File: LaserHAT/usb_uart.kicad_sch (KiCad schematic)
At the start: 9 parts

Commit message: Updates with lots of manual work
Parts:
- removed C_USB1, C_USB2: 100nF, Capacitor_SMD:C_0402_1005Metric, symbol Device:C
- removed J_USB: USB_C_Receptacle, Connector_USB:USB_C_Receptacle_GCT_USB4125, symbol Connector_USB:USB_C_Receptacle_USB2.0
- removed R_CC1, R_CC2: 5k1, Resistor_SMD:R_0402_1005Metric, symbol Device:R
- removed R_SHIELD: 1M, Resistor_SMD:R_0402_1005Metric, symbol Device:R
- removed SB1: SB1_bridge, Jumper:SolderJumper-2_P1.3mm_Open_RoundedPad1.0x1.5mm, symbol Jumper:SolderJumper_2_Open
- removed SB2: SB2_bridge, Jumper:SolderJumper-2_P1.3mm_Open_RoundedPad1.0x1.5mm, symbol Jumper:SolderJumper_2_Open
- removed U_USB: CH340N, Package_SO:SOIC-8_3.9x4.9mm_P1.27mm, symbol Interface_USB:CH340N
- added C5, C6: 100nF, Capacitor_SMD:C_0402_1005Metric, symbol Device:C_Small
- added J5: USB_C_Receptacle_USB2.0_16P, symbol Connector:USB_C_Receptacle_USB2.0_16P
- added R10, R8: 5.1K, Resistor_SMD:R_0402_1005Metric, symbol Device:R
- added U6: CH340N, Package_SO:JEITA_SOIC-8_3.9x4.9mm_P1.27mm, symbol Interface_USB:CH340N
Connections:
- net GND: now also C5.1, C6.2, J5.A1 (GND), J5.A12 (GND), J5.B1 (GND), J5.B12 (GND), J5.S1 (SHIELD), R10.2, R8.2, U6.3 (GND)
- new net: J5.B5 (CC2), R10.1
- new net: J5.A6 (D+), J5.B6 (D+), U6.1 (UD+)
- new net: J5.A7 (D-), J5.B7 (D-), U6.2 (UD-)
- new net: C5.2, U6.8 (V3)
- new net: J5.A5 (CC1), R8.1
- new net +3.3V: C6.1, U6.5 (VCC)
- new net +5V: J5.A4 (VBUS), J5.A9 (VBUS), J5.B4 (VBUS), J5.B9 (VBUS)
- new net CH340_RTS: U6.4 (~{RTS})
- new net CH340_RX: U6.7 (RXD)
- new net CH340_TX: U6.6 (TXD)
- no-connect marks 3 -> 0

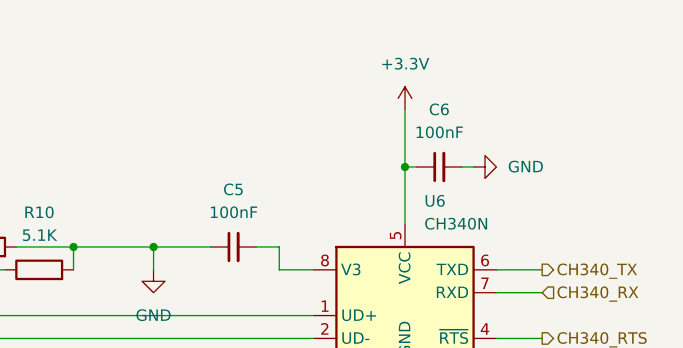
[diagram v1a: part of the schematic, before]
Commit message: Updates to design, finalized PCB layout
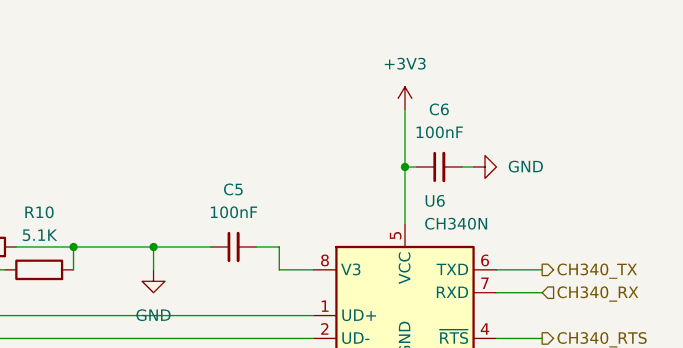
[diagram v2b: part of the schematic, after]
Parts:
- J5: footprint (none) -> Connector_USB:USB_C_Receptacle_G-Switch_GT-USB-7010ASV
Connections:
- net +3.3V renamed +3V3
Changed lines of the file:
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@@
 			)
 		)
-		(property "Value" "+3.3V"
+		(property "Value" "+3V3"
 			(at 173.99 76.2 0)
 			(effects
@@
 			)
 		)
-		(property "Footprint" ""
+		(property "Footprint" "Connector_USB:USB_C_Receptacle_G-Switch_GT-USB-7010ASV"
 			(at 111.76 106.68 0)
 			(effects

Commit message: Updated project for manufacturing. Should merge branch if/when we get back a working product
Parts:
- C5, C6: LCSC Part # (none) -> C307331
- J5: LCSC Part # (none) -> C2927038; LCSC Part# C2927038 -> (none)
- R10, R8: value 5.1K -> 5.1k; LCSC Part # (none) -> C25905
- U6: LCSC Part # (none) -> C2977777; LCSC Part# C2977777 -> (none)
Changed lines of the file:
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@@
 			)
 		)
-		(property "Description" "Unpolarized capacitor, small symbol"
+		(property "Description" "100nF ±10% 50V Ceramic Capacitor X7R 0402"
 			(at 177.8 87.63 0)
+			(effects
+				(font
+					(size 1.27 1.27)
+				)
+				(hide yes)
+			)
+		)
+		(property "LCSC Part #" "C307331"
+			(at 177.8 87.63 90)
 			(effects
 				(font
@@
 			)
 		)
-		(property "Value" "5.1K"
+		(property "Value" "5.1k"
 			(at 133.35 95.25 90)
 			(effects
@@
 			)
 		)
-		(property "Description" "Resistor"
+		(property "Description" "5.1kΩ 100mW Thick Film Resistor ±100ppm/℃ ±1% 0402 Chip Resistor - Surface Mount RoHS"
 			(at 133.35 99.06 0)
+			(effects
+				(font
+					(size 1.27 1.27)
+				)
+				(hide yes)
+			)
+		)
+		(property "LCSC Part #" "C25905"
+			(at 133.35 99.06 90)
 			(effects
 				(font
@@
 			)
 		)
-		(property "LCSC Part#" "C2977777"
+		(property "LCSC Part #" "C2977777"
 			(at 173.99 101.6 0)
 			(effects
@@
 			)
 		)
-		(property "Description" "Unpolarized capacitor, small symbol"
+		(property "Description" "100nF ±10% 50V Ceramic Capacitor X7R 0402"
 			(at 154.94 96.52 0)
+			(effects
+				(font
+					(size 1.27 1.27)
+				)
+				(hide yes)
+			)
+		)
+		(property "LCSC Part #" "C307331"
+			(at 154.94 96.52 90)
 			(effects
 				(font
@@
 			)
 		)
-		(property "LCSC Part#" "C2927038"
+		(property "LCSC Part #" "C2927038"
 			(at 107.95 106.68 0)
 			(effects
@@
 			)
 		)
-		(property "Value" "5.1K"
+		(property "Value" "5.1k"
 			(at 127 92.71 90)
 			(effects
@@
 			)
 		)
-		(property "Description" "Resistor"
+		(property "Description" "5.1kΩ 100mW Thick Film Resistor ±100ppm/℃ ±1% 0402 Chip Resistor - Surface Mount RoHS"
 			(at 127 96.52 0)
 			(effects
 				(font
+					(size 1.27 1.27)
+				)
+				(hide yes)
+			)
+		)
+		(property "LCSC Part #" "C25905"
+			(at 127 96.52 90)
+			(effects
+				(font
